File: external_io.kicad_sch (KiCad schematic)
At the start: 13 parts, among them J1 UJ20-C-H-G-SMT-1-P16-TR, J3 Conn_01x02_Socket, J4 Conn_01x04_Socket, J5 Conn_01x03_Socket, J6 Conn_01x03_Socket, J7 Conn_01x03_Socket, U1 USBLC6-2SC6, U2 USBLC6-2SC6

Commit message: Did a lot of routing
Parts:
- TP1, TP2, TP3: footprint TestPoint:TestPoint_Keystone_5015_Micro_Mini -> _BMS:Harwin TP
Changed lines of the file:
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@@
 			)
 		)
-		(property "Footprint" "TestPoint:TestPoint_Keystone_5015_Micro_Mini"
+		(property "Footprint" "_BMS:Harwin TP"
 			(at 118.11 87.63 0)
 			(effects
@@
 		(dnp no)
 		(property "Reference" "TP2"
-			(at 123.952 77.47 90)
+			(at 123.952 78.232 90)
 			(effects
 				(font
@@
 		)
 		(property "Value" "TestPoint"
-			(at 123.952 80.01 90)
+			(at 123.952 80.772 90)
 			(effects
 				(font
@@
 			)
 		)
-		(property "Footprint" "TestPoint:TestPoint_Keystone_5015_Micro_Mini"
+		(property "Footprint" "_BMS:Harwin TP"
 			(at 118.11 85.09 0)
 			(effects
@@
 	)
 	(symbol
-		(lib_id "Connector:TestPoint")
-		(at 118.11 77.47 270)
-		(unit 1)
-		(exclude_from_sim no)
-		(in_bom yes)
-		(on_board yes)
-		(dnp no)
-		(property "Reference" "TP1"
-			(at 123.952 72.136 90)
-			(effects
-				(font
-					(size 1.27 1.27)
-				)
-				(justify left)
-			)
-		)
-		(property "Value" "TestPoint"
-			(at 123.952 74.676 90)
-			(effects
-				(font
-					(size 1.27 1.27)
-				)
-				(justify left)
-			)
-		)
-		(property "Footprint" "TestPoint:TestPoint_Keystone_5015_Micro_Mini"
-			(at 118.11 82.55 0)
-			(effects
-				(font
-					(size 1.27 1.27)
-				)
-				(hide yes)
-			)
-		)
-		(property "Datasheet" "~"
-			(at 118.11 82.55 0)
-			(effects
-				(font
-					(size 1.27 1.27)
-				)
-				(hide yes)
-			)
-		)
-		(property "Description" "test point"
-			(at 118.11 77.47 0)
-			(effects
-				(font
-					(size 1.27 1.27)
-				)
-				(hide yes)
-			)
-		)
-		(property "Mfr" ""
-			(at 118.11 77.47 0)
-			(effects
-				(font
-					(size 1.27 1.27)
-				)
-				(hide yes)
-			)
-		)
-		(property "Mfr P/N" ""
-			(at 118.11 77.47 0)
-			(effects
-				(font
-					(size 1.27 1.27)
-				)
-				(hide yes)
-			)
-		)
-		(property "Supplier_1" ""
-			(at 118.11 77.47 0)
-			(effects
-				(font
-					(size 1.27 1.27)
-				)
-				(hide yes)
-			)
-		)
-		(property "Supplier_1 P/N" ""
-			(at 118.11 77.47 0)
-			(effects
-				(font
-					(size 1.27 1.27)
-				)
-				(hide yes)
-			)
-		)
-		(property "Supplier_1 Unit Price" ""
-			(at 118.11 77.47 0)
-			(effects
-				(font
-					(size 1.27 1.27)
-				)
-				(hide yes)
-			)
-		)
-		(property "Supplier_1 Price @ Qty" ""
-			(at 118.11 77.47 0)
-			(effects
-				(font
-					(size 1.27 1.27)
-				)
-				(hide yes)
-			)
-		)
-		(property "Supplier_2" ""
-			(at 118.11 77.47 0)
-			(effects
-				(font
-					(size 1.27 1.27)
-				)
-				(hide yes)
-			)
-		)
-		(property "Supplier_2 P/N" ""
-			(at 118.11 77.47 0)
-			(effects
-				(font
-					(size 1.27 1.27)
-				)
-				(hide yes)
-			)
-		)
-		(property "Supplier_2 Unit Price" ""
-			(at 118.11 77.47 0)
-			(effects
-				(font
-					(size 1.27 1.27)
-				)
-				(hide yes)
-			)
-		)
-		(property "Supplier_2 Price @ Qty" ""
-			(at 118.11 77.47 0)
-			(effects
-				(font
-					(size 1.27 1.27)
-				)
-				(hide yes)
-			)
-		)
-		(pin "1"
-		)
-		(instances
-			(project ""
-				(path "/124184ba-5d68-4d9f-8da6-acc6720ab30b/93f9b420-7cce-46a9-9201-666f07a18f85/2982e12c-39cd-4158-a648-a90b7f6b527c"
-					(reference "TP1")
-					(unit 1)
-				)
-			)
-		)
-	)
-	(symbol
 		(lib_id "Connector:Conn_01x02_Socket")
 		(at 140.97 138.43 0)
@@
 					(unit 1)
 				)
+			)
+		)
+	)
+	(symbol
+		(lib_id "Connector:TestPoint")
+		(at 118.11 77.47 270)
+		(unit 1)
+		(exclude_from_sim no)
+		(in_bom yes)
+		(on_board yes)
+		(dnp no)
+		(property "Reference" "TP1"
+			(at 123.952 73.66 90)
+			(effects
+				(font
+					(size 1.27 1.27)
+				)
+				(justify left)
+			)
+		)
+		(property "Value" "TestPoint"
+			(at 123.952 76.2 90)
+			(effects
+				(font
+					(size 1.27 1.27)
+				)
+				(justify left)
+			)
+		)
+		(property "Footprint" "_BMS:Harwin TP"
+			(at 118.11 82.55 0)
+			(effects
+				(font
+					(size 1.27 1.27)
+				)
+				(hide yes)
+			)
+		)
+		(property "Datasheet" "~"
+			(at 118.11 82.55 0)
+			(effects
+				(font
+					(size 1.27 1.27)
+				)
+				(hide yes)
+			)
+		)
+		(property "Description" "test point"
+			(at 118.11 77.47 0)
+			(effects
+				(font
+					(size 1.27 1.27)
+				)
+				(hide yes)
+			)
+		)
+		(property "Mfr" ""
+			(at 118.11 77.47 0)
+			(effects
+				(font
+					(size 1.27 1.27)
+				)
+				(hide yes)
+			)
+		)
+		(property "Mfr P/N" ""
+			(at 118.11 77.47 0)
+			(effects
+				(font
+					(size 1.27 1.27)
+				)
+				(hide yes)
+			)
+		)
+		(property "Supplier_1" ""
+			(at 118.11 77.47 0)
+			(effects
+				(font
+					(size 1.27 1.27)
+				)
+				(hide yes)
+			)
+		)
+		(property "Supplier_1 P/N" ""
+			(at 118.11 77.47 0)
+			(effects
+				(font
+					(size 1.27 1.27)
+				)
+				(hide yes)
+			)
+		)
+		(property "Supplier_1 Unit Price" ""
+			(at 118.11 77.47 0)
+			(effects
+				(font
+					(size 1.27 1.27)
+				)
+				(hide yes)
+			)
+		)
+		(property "Supplier_1 Price @ Qty" ""
+			(at 118.11 77.47 0)
+			(effects
+				(font
+					(size 1.27 1.27)
+				)
+				(hide yes)
+			)
+		)
+		(property "Supplier_2" ""
+			(at 118.11 77.47 0)
+			(effects
+				(font
+					(size 1.27 1.27)
+				)
+				(hide yes)
+			)
+		)
+		(property "Supplier_2 P/N" ""
+			(at 118.11 77.47 0)
+			(effects
+				(font
+					(size 1.27 1.27)
+				)
+				(hide yes)
+			)
+		)
+		(property "Supplier_2 Unit Price" ""
+			(at 118.11 77.47 0)
+			(effects
+				(font
+					(size 1.27 1.27)
+				)
+				(hide yes)
+			)
+		)
+		(property "Supplier_2 Price @ Qty" ""
+			(at 118.11 77.47 0)
+			(effects
+				(font
+					(size 1.27 1.27)
+				)
+				(hide yes)
+			)
+		)
+		(pin "1"
+		)
+		(instances
+			(project "BMS"
+				(path "/124184ba-5d68-4d9f-8da6-acc6720ab30b/93f9b420-7cce-46a9-9201-666f07a18f85/2982e12c-39cd-4158-a648-a90b7f6b527c"
+					(reference "TP1")
+					(unit 1)
+				)

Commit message: Pushing
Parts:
- added D24, D27: LED, symbol Device:LED
- added FB1, FB2: 120Ω@100MHz, Inductor_SMD:L_0603_1608Metric, symbol Device:FerriteBead_Small
- added R37, R40: R, symbol Device:R
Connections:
- net EXT_5V: now also FB1.1; no longer J4.4 (Pin_4)
- net GND: now also D24.1 (K), D27.1 (K)
- net V_USB: now also FB2.1; no longer J1.A4_B9 (VBUS), J1.B4_A9 (VBUS__1)
- new net: FB1.2, J4.4 (Pin_4), R37.2
- new net: FB2.2, J1.A4_B9 (VBUS), J1.B4_A9 (VBUS__1), R40.2
- new net: D24.2 (A), R37.1
- new net: D27.2 (A), R40.1
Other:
- note added: "Main pack connector"
- moved on the sheet: J1, J4, J5, J6, J7, R1, R2, TP1, TP2, TP3, U1

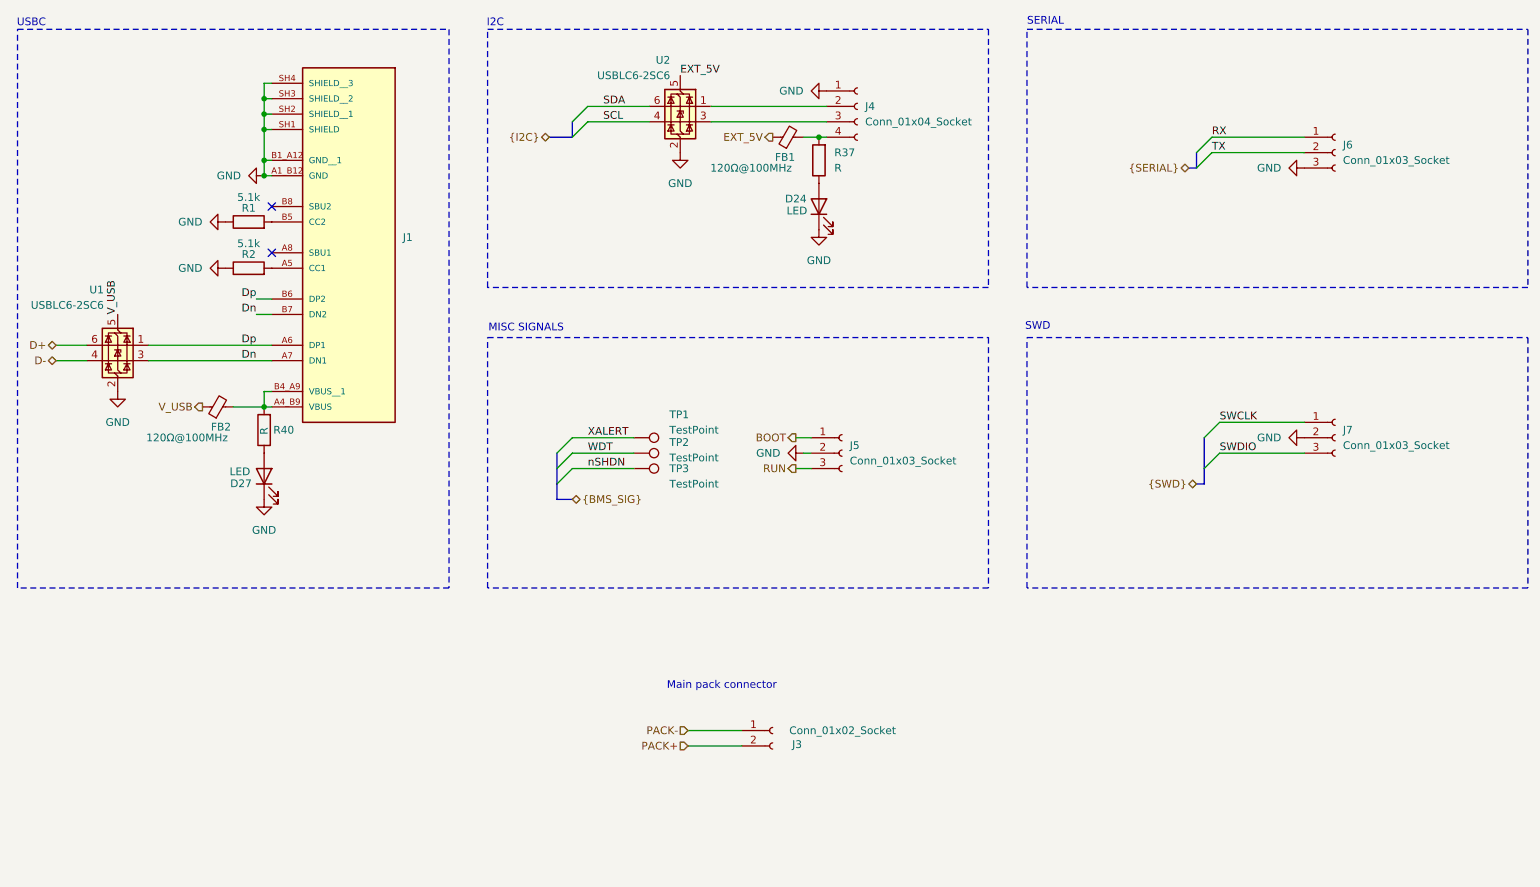
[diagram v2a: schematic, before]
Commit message: Adding in signals and cleaning up schematic
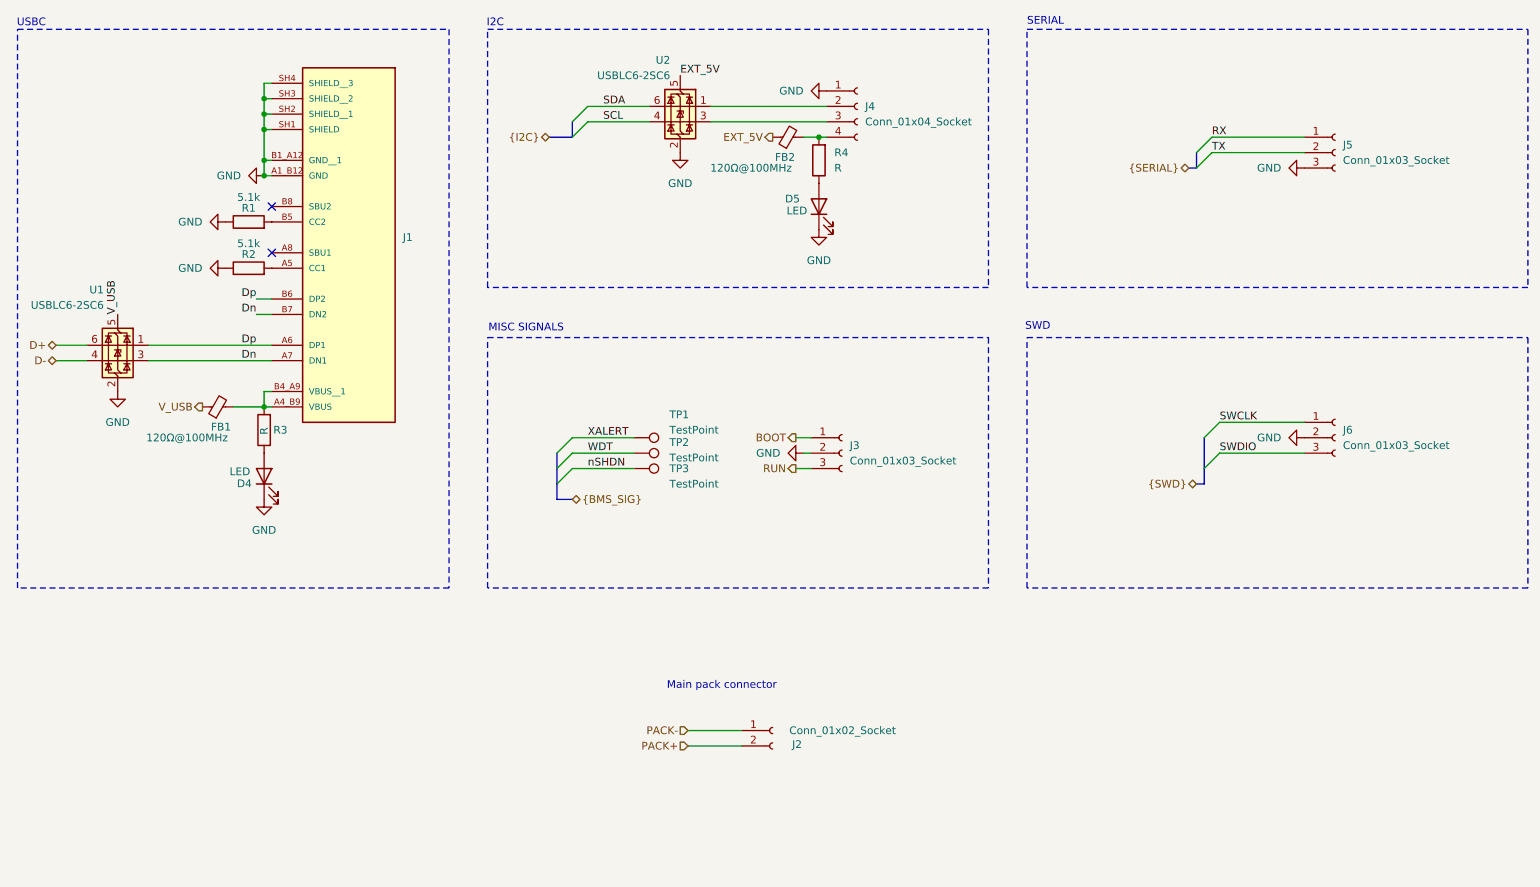
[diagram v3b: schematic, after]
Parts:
- renumbered D27 to D4, D24 to D5, FB2 to FB1, FB1 to FB2, J3 to J2, J5 to J3, J6 to J5, J7 to J6, R40 to R3, R37 to R4
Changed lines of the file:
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@@
 		(on_board yes)
 		(dnp no)
-		(property "Reference" "FB1"
+		(property "Reference" "FB2"
 			(at 143.002 43.942 90)
 			(effects
@@
 			(project ""
 				(path "/124184ba-5d68-4d9f-8da6-acc6720ab30b/93f9b420-7cce-46a9-9201-666f07a18f85/2982e12c-39cd-4158-a648-a90b7f6b527c"
-					(reference "FB1")
+					(reference "FB2")
 					(unit 1)
 				)
@@
 		(dnp no)
 		(fields_autoplaced yes)
-		(property "Reference" "J5"
+		(property "Reference" "J3"
 			(at 153.67 91.4399 0)
 			(effects
@@
 			(project "BMS"
 				(path "/124184ba-5d68-4d9f-8da6-acc6720ab30b/93f9b420-7cce-46a9-9201-666f07a18f85/2982e12c-39cd-4158-a648-a90b7f6b527c"
-					(reference "J5")
+					(reference "J3")
 					(unit 1)
 				)
@@
 		(dnp no)
 		(fields_autoplaced yes)
-		(property "Reference" "#PWR090"
+		(property "Reference" "#PWR010"
 			(at 148.59 62.23 0)
 			(effects
@@
 			(project "BMS"
 				(path "/124184ba-5d68-4d9f-8da6-acc6720ab30b/93f9b420-7cce-46a9-9201-666f07a18f85/2982e12c-39cd-4158-a648-a90b7f6b527c"
-					(reference "#PWR090")
+					(reference "#PWR010")
 					(unit 1)
 				)
@@
 		(on_board yes)
 		(dnp no)
-		(property "Reference" "#PWR03"
+		(property "Reference" "#PWR05"
 			(at 44.45 62.23 0)
 			(effects
@@
 			(project "BMS"
 				(path "/124184ba-5d68-4d9f-8da6-acc6720ab30b/93f9b420-7cce-46a9-9201-666f07a18f85/2982e12c-39cd-4158-a648-a90b7f6b527c"
-					(reference "#PWR03")
+					(reference "#PWR05")
 					(unit 1)
 				)
@@
 		(dnp no)
 		(fields_autoplaced yes)
-		(property "Reference" "#PWR06"
+		(property "Reference" "#PWR09"
 			(at 139.7 92.71 0)
 			(effects
@@
 			(project ""
 				(path "/124184ba-5d68-4d9f-8da6-acc6720ab30b/93f9b420-7cce-46a9-9201-666f07a18f85/2982e12c-39cd-4158-a648-a90b7f6b527c"
-					(reference "#PWR06")
+					(reference "#PWR09")
 					(unit 1)
 				)
@@
 		(dnp no)
 		(fields_autoplaced yes)
-		(property "Reference" "R37"
+		(property "Reference" "R4"
 			(at 151.13 43.1799 0)
 			(effects
@@
 			(project "BMS"
 				(path "/124184ba-5d68-4d9f-8da6-acc6720ab30b/93f9b420-7cce-46a9-9201-666f07a18f85/2982e12c-39cd-4158-a648-a90b7f6b527c"
-					(reference "R37")
+					(reference "R4")
 					(unit 1)
 				)
@@
 		(dnp no)
 		(fields_autoplaced yes)
-		(property "Reference" "#PWR07"
+		(property "Reference" "#PWR011"
 			(at 143.51 33.02 0)
 			(effects
@@
 			(project "BMS"
 				(path "/124184ba-5d68-4d9f-8da6-acc6720ab30b/93f9b420-7cce-46a9-9201-666f07a18f85/2982e12c-39cd-4158-a648-a90b7f6b527c"
-					(reference "#PWR07")
+					(reference "#PWR011")
 					(unit 1)
 				)
@@
 		(on_board yes)
 		(dnp no)
-		(property "Reference" "D24"
+		(property "Reference" "D5"
 			(at 143.002 50.8 90)
 			(effects
@@
 			(project "BMS"
 				(path "/124184ba-5d68-4d9f-8da6-acc6720ab30b/93f9b420-7cce-46a9-9201-666f07a18f85/2982e12c-39cd-4158-a648-a90b7f6b527c"
-					(reference "D24")
+					(reference "D5")
 					(unit 1)
 				)
@@
 		(dnp no)
 		(fields_autoplaced yes)
-		(property "Reference" "#PWR05"
+		(property "Reference" "#PWR08"
 			(at 125.73 49.53 0)
 			(effects
@@
 			(project "BMS"
 				(path "/124184ba-5d68-4d9f-8da6-acc6720ab30b/93f9b420-7cce-46a9-9201-666f07a18f85/2982e12c-39cd-4158-a648-a90b7f6b527c"
-					(reference "#PWR05")
+					(reference "#PWR08")
 					(unit 1)
 				)
@@
 		(dnp no)
 		(fields_autoplaced yes)
-		(property "Reference" "#PWR093"
+		(property "Reference" "#PWR07"
 			(at 57.15 106.68 0)
 			(effects
@@
 			(project "BMS"
 				(path "/124184ba-5d68-4d9f-8da6-acc6720ab30b/93f9b420-7cce-46a9-9201-666f07a18f85/2982e12c-39cd-4158-a648-a90b7f6b527c"
-					(reference "#PWR093")
+					(reference "#PWR07")
 					(unit 1)
 				)
@@
 		(on_board yes)
 		(dnp no)
-		(property "Reference" "D27"
+		(property "Reference" "D4"
 			(at 55.118 97.7266 90)
 			(effects
@@
 			(project "BMS"
 				(path "/124184ba-5d68-4d9f-8da6-acc6720ab30b/93f9b420-7cce-46a9-9201-666f07a18f85/2982e12c-39cd-4158-a648-a90b7f6b527c"
-					(reference "D27")
+					(reference "D4")
 					(unit 1)
 				)
@@
 		(on_board yes)
 		(dnp no)
-		(property "Reference" "#PWR04"
+		(property "Reference" "#PWR06"
 			(at 50.8 46.99 0)
 			(effects
@@
 			(project "BMS"
 				(path "/124184ba-5d68-4d9f-8da6-acc6720ab30b/93f9b420-7cce-46a9-9201-666f07a18f85/2982e12c-39cd-4158-a648-a90b7f6b527c"
-					(reference "#PWR04")
+					(reference "#PWR06")
 					(unit 1)
 				)
@@
 		(dnp no)
 		(fields_autoplaced yes)
-		(property "Reference" "J7"
+		(property "Reference" "J6"
 			(at 234.95 88.8999 0)
 			(effects
@@
 			(project "BMS"
 				(path "/124184ba-5d68-4d9f-8da6-acc6720ab30b/93f9b420-7cce-46a9-9201-666f07a18f85/2982e12c-39cd-4158-a648-a90b7f6b527c"
-					(reference "J7")
+					(reference "J6")
 					(unit 1)
 				)
@@
 		(on_board yes)
 		(dnp no)
-		(property "Reference" "FB2"
+		(property "Reference" "FB1"
 			(at 50.038 88.392 90)
 			(effects
@@
 			(project "BMS"
 				(path "/124184ba-5d68-4d9f-8da6-acc6720ab30b/93f9b420-7cce-46a9-9201-666f07a18f85/2982e12c-39cd-4158-a648-a90b7f6b527c"
-					(reference "FB2")
+					(reference "FB1")
 					(unit 1)
 				)
@@
 		(dnp no)
 		(fields_autoplaced yes)
-		(property "Reference" "#PWR09"
+		(property "Reference" "#PWR013"
 			(at 222.25 90.17 0)
 			(effects
@@
 			(project "BMS"
 				(path "/124184ba-5d68-4d9f-8da6-acc6720ab30b/93f9b420-7cce-46a9-9201-666f07a18f85/2982e12c-39cd-4158-a648-a90b7f6b527c"
-					(reference "#PWR09")
+					(reference "#PWR013")
 					(unit 1)
 				)
@@
 		(on_board yes)
 		(dnp no)
-		(property "Reference" "R40"
+		(property "Reference" "R3"
 			(at 58.674 88.9 0)
 			(effects
@@
 			(project "BMS"
 				(path "/124184ba-5d68-4d9f-8da6-acc6720ab30b/93f9b420-7cce-46a9-9201-666f07a18f85/2982e12c-39cd-4158-a648-a90b7f6b527c"
-					(reference "R40")
+					(reference "R3")
 					(unit 1)
 				)
@@
 		(on_board yes)
 		(dnp no)
-		(property "Reference" "J3"
+		(property "Reference" "J2"
 			(at 145.796 140.716 0)
 			(effects
@@
 			(project "BMS"
 				(path "/124184ba-5d68-4d9f-8da6-acc6720ab30b/93f9b420-7cce-46a9-9201-666f07a18f85/2982e12c-39cd-4158-a648-a90b7f6b527c"
-					(reference "J3")
+					(reference "J2")
 					(unit 1)
 				)
@@
 		(dnp no)
 		(fields_autoplaced yes)
-		(property "Reference" "J6"
+		(property "Reference" "J5"
 			(at 234.95 41.9099 0)
 			(effects
@@
 			(project ""
 				(path "/124184ba-5d68-4d9f-8da6-acc6720ab30b/93f9b420-7cce-46a9-9201-666f07a18f85/2982e12c-39cd-4158-a648-a90b7f6b527c"
-					(reference "J6")
+					(reference "J5")
 					(unit 1)
 				)
@@
 		(dnp no)
 		(fields_autoplaced yes)
-		(property "Reference" "#PWR01"
+		(property "Reference" "#PWR03"
 			(at 33.02 88.9 0)
 			(effects
@@
 			(project "BMS"
 				(path "/124184ba-5d68-4d9f-8da6-acc6720ab30b/93f9b420-7cce-46a9-9201-666f07a18f85/2982e12c-39cd-4158-a648-a90b7f6b527c"
-					(reference "#PWR01")
+					(reference "#PWR03")
 					(unit 1)
 				)
@@
 		(dnp no)
 		(fields_autoplaced yes)
-		(property "Reference" "#PWR08"
+		(property "Reference" "#PWR012"
 			(at 222.25 45.72 0)
 			(effects
@@
 			(project "BMS"
 				(path "/124184ba-5d68-4d9f-8da6-acc6720ab30b/93f9b420-7cce-46a9-9201-666f07a18f85/2982e12c-39cd-4158-a648-a90b7f6b527c"
-					(reference "#PWR08")
+					(reference "#PWR012")
 					(unit 1)
 				)
@@
 		(on_board yes)
 		(dnp no)
-		(property "Reference" "#PWR02"
+		(property "Reference" "#PWR04"
 			(at 44.45 54.61 0)
 			(effects
@@
 			(project "BMS"
 				(path "/124184ba-5d68-4d9f-8da6-acc6720ab30b/93f9b420-7cce-46a9-9201-666f07a18f85/2982e12c-39cd-4158-a648-a90b7f6b527c"
-					(reference "#PWR02")
+					(reference "#PWR04")
 					(unit 1)
 				)
